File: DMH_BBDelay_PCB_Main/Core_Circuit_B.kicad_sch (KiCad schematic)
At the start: 70 parts, among them Q8 J113, SW1 SW_DPDT_OnOffOn_x2, SW2 SW_DPDT_x2, SW4 SW_SPDT, U5 TL074, U6 TL074, U7 V3205, U8 CD4046, U9 40106

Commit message: Re-implemented Ping Pong mode with CD4053
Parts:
- removed SW1: SW_DPDT_OnOffOn_x2, SynthStuff:Toggle_Switch_2_Poles_TE, symbol SynthStuff:SW_DPDT_OnOffOn_x2
- added R170: 100k, Resistor_THT:R_Axial_DIN0207_L6.3mm_D2.5mm_P7.62mm_Horizontal, symbol Device:R_US
- added SW1: SW_SPDT, symbol Switch:SW_SPDT
- added U18: CD4053B, Package_DIP:DIP-16_W7.62mm_Socket, symbol Analog_Switch:CD4053B
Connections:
- net +12V: now also R170.2, U18.16 (VDD)
- net -12V: now also U18.7 (VEE)
- net GND: now also SW1.1 (A), U18.6 (INH), U18.8 (VSS)
- net W_B_Out_m: now also U18.1 (B1), U18.12 (A0)
- net D_B_m renamed B_In_Buff_m
- net B_In_Buff_m: now also U18.3 (C1); no longer R25.1
- new net B_In_Buff_Sw_m: R25.1, U18.4 (C)
- new net PP_Sw_c: SW1.2 (B)
- new net PP_Sw_m: R170.1, U18.10 (S2), U18.11 (S1), U18.9 (S3)
- new net VCA_FB_A_In_m: U18.14 (A)
- new net VCA_FB_B_In_m: U18.15 (B)
- new net W_A_Out_m: U18.13 (A1), U18.2 (B0)
- no-connect marks 13 -> 15
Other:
- moved on the sheet: C30, C31, C33, C34, D16, D17, D18, R157, R158, R159, SW2B, U5E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

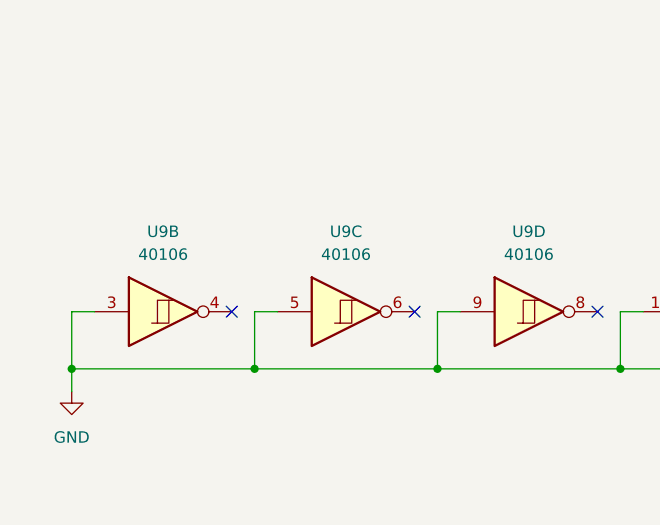
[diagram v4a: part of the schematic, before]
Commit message: Added schmit triggers to inhibt CV input paths
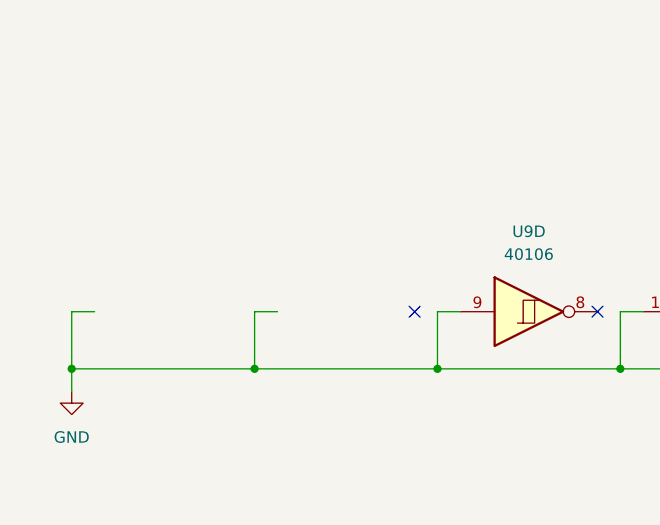
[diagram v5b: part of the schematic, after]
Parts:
- removed unit 2 of U9
- removed unit 3 of U9
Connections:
- no-connect marks 15 -> 14
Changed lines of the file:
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@@
 	)
 	(no_connect
-		(at 36.83 254)
-	)
-	(no_connect
 		(at 241.3 226.06)
 	)
@@
 	)
 	(symbol
-		(lib_id "4xxx:40106")
-		(at 29.21 254 0)
-		(unit 2)
-		(body_style 1)
-		(exclude_from_sim no)
-		(in_bom yes)
-		(on_board yes)
-		(in_pos_files yes)
-		(dnp no)
-		(fields_autoplaced yes)
-		(property "Reference" "U9"
-			(at 29.21 245.11 0)
-			(show_name no)
-			(do_not_autoplace no)
-			(effects
-				(font
-					(size 1.27 1.27)
-				)
-			)
-		)
-		(property "Value" "40106"
-			(at 29.21 247.65 0)
-			(show_name no)
-			(do_not_autoplace no)
-			(effects
-				(font
-					(size 1.27 1.27)
-				)
-			)
-		)
-		(property "Footprint" "Package_DIP:DIP-14_W7.62mm_Socket"
-			(at 29.21 254 0)
-			(hide yes)
-			(show_name no)
-			(do_not_autoplace no)
-			(effects
-				(font
-					(size 1.27 1.27)
-				)
-			)
-		)
-		(property "Datasheet" "https://assets.nexperia.com/documents/data-sheet/HEF40106B.pdf"
-			(at 29.21 254 0)
-			(hide yes)
-			(show_name no)
-			(do_not_autoplace no)
-			(effects
-				(font
-					(size 1.27 1.27)
-				)
-			)
-		)
-		(property "Description" "Hex Schmitt trigger inverter"
-			(at 29.21 254 0)
-			(hide yes)
-			(show_name no)
-			(do_not_autoplace no)
-			(effects
-				(font
-					(size 1.27 1.27)
-				)
-			)
-		)
-		(pin "3"
-		)
-		(pin "11"
-		)
-		(pin "9"
-		)
-		(pin "12"
-		)
-		(pin "2"
-		)
-		(pin "6"
-		)
-		(pin "13"
-		)
-		(pin "14"
-		)
-		(pin "4"
-		)
-		(pin "8"
-		)
-		(pin "1"
-		)
-		(pin "5"
-		)
-		(pin "10"
-		)
-		(pin "7"
-		)
-		(instances
-			(project "DMH_BBDelay_PCB_Main"
-				(path "/58f4306d-5387-4983-bb08-41a2313fd315/53120047-129a-4e0f-876f-6cafa2f18733"
-					(reference "U9")
-					(unit 2)
-				)
-			)
-		)
-	)
-	(symbol
 		(lib_id "power:+5V")
 		(at 140.97 78.74 0)
@@
 				)
 			)
-		)
-	)
-	(symbol
-		(lib_id "4xxx:40106")
-		(at 49.53 254 0)
-		(unit 3)
-		(body_style 1)
-		(exclude_from_sim no)
-		(in_bom yes)
-		(on_board yes)
-		(in_pos_files yes)
-		(dnp no)
-		(fields_autoplaced yes)
-		(property "Reference" "U9"
-			(at 49.53 245.11 0)
-			(show_name no)
-			(do_not_autoplace no)
-			(effects
-				(font
-					(size 1.27 1.27)
-				)
-			)
-		)
-		(property "Value" "40106"
-			(at 49.53 247.65 0)
-			(show_name no)
-			(do_not_autoplace no)
-			(effects
-				(font
-					(size 1.27 1.27)
-				)
-			)
-		)
-		(property "Footprint" "Package_DIP:DIP-14_W7.62mm_Socket"
-			(at 49.53 254 0)
-			(hide yes)
-			(show_name no)
-			(do_not_autoplace no)
-			(effects
-				(font
-					(size 1.27 1.27)
-				)
-			)
-		)
-		(property "Datasheet" "https://assets.nexperia.com/documents/data-sheet/HEF40106B.pdf"
-			(at 49.53 254 0)
-			(hide yes)
-			(show_name no)
-			(do_not_autoplace no)
-			(effects
-				(font
-					(size 1.27 1.27)
-				)
-			)
-		)
-		(property "Description" "Hex Schmitt trigger inverter"
-			(at 49.53 254 0)
-			(hide yes)
-			(show_name no)
-			(do_not_autoplace no)
-			(effects
-				(font
-					(size 1.27 1.27)
-				)
-			)
-		)
-		(pin "3"
-		)
-		(pin "11"
-		)
-		(pin "9"
-		)
-		(pin "12"
-		)
-		(pin "2"
-		)
-		(pin "6"
-		)
-		(pin "13"
-		)
-		(pin "14"
-		)
-		(pin "4"
-		)
-		(pin "8"
-		)
-		(pin "1"
-		)
-		(pin "5"
-		)
-		(pin "10"
-		)
-		(pin "7"
-		)
-		(instances
-			(project "DMH_BBDelay_PCB_Main"
-				(path "/58f4306d-5387-4983-bb08-41a2313fd315/53120047-129a-4e0f-876f-6cafa2f18733"
-					(reference "U9")
-					(unit 3)
-				)
-			)

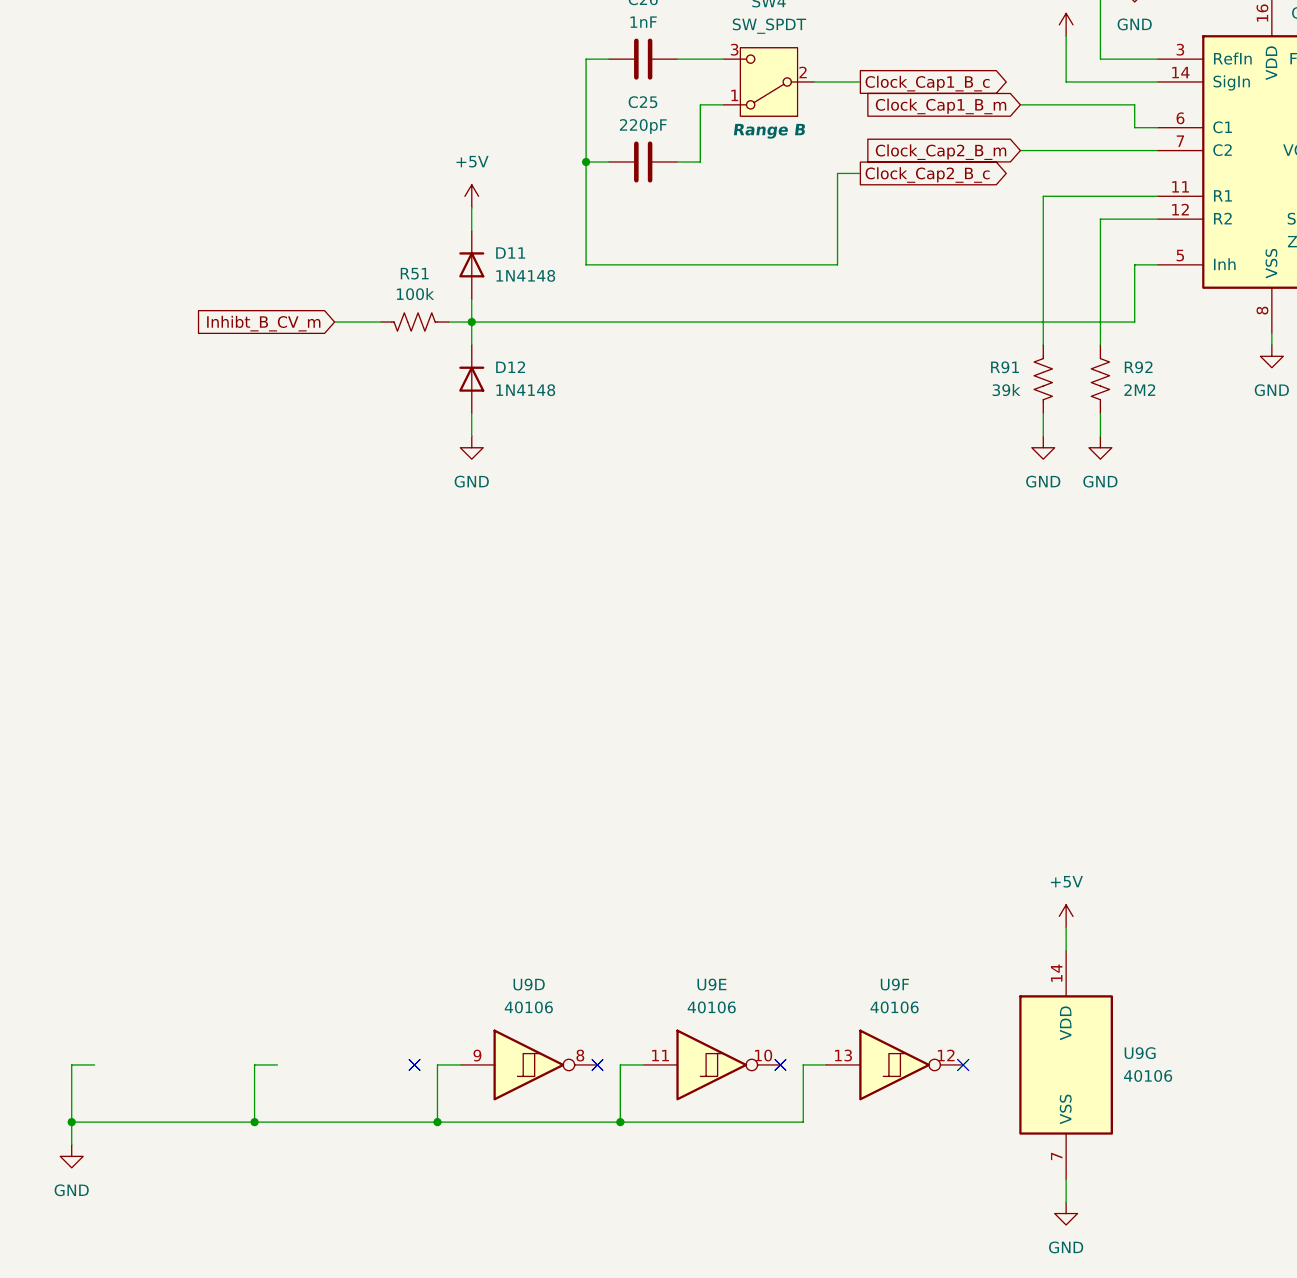
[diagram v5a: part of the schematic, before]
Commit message: Schmitt triggers added to Inhibt CV input paths
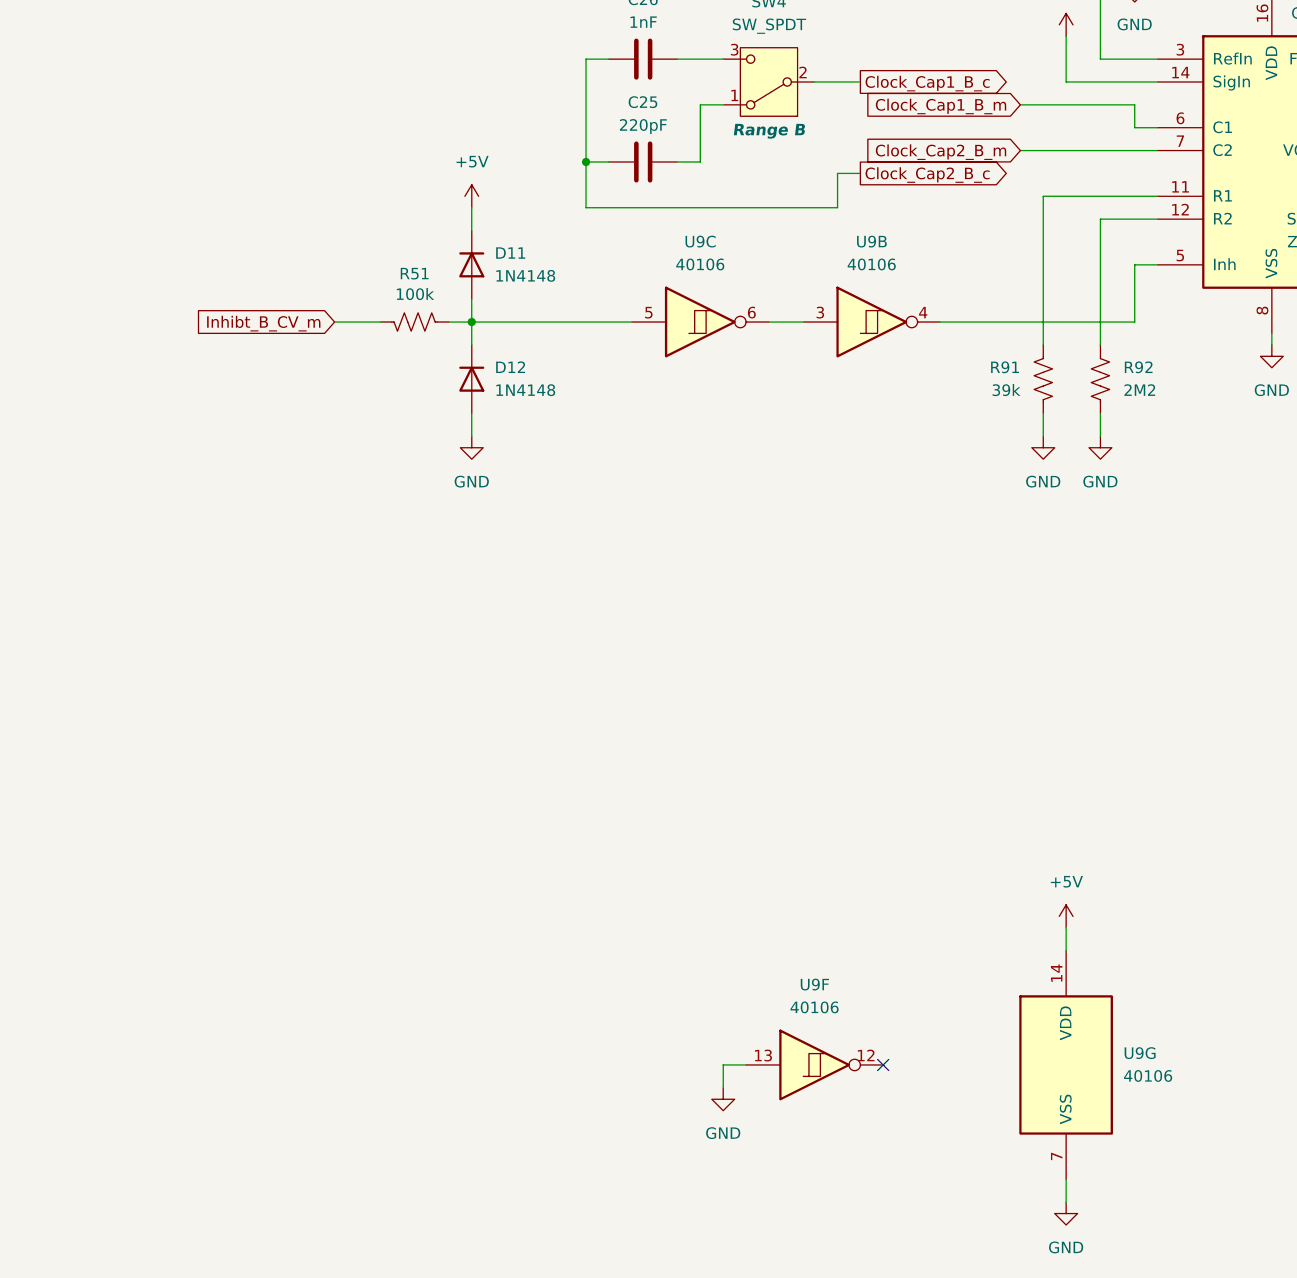
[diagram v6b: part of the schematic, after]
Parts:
- removed unit 4 of U9
- removed unit 5 of U9
- added unit 3 of U9
- added unit 2 of U9
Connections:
- net at D11.2 (A), D12.1 (K), R51.2: now also U9.5; no longer U8.5 (Inh)
- new net: U9.3, U9.6
- new net: U8.5 (Inh), U9.4
- no-connect marks 14 -> 11
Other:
- moved on the sheet: U9F

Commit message: Added TRS jacks to IO page
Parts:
- added R172: 100k, Resistor_THT:R_Axial_DIN0207_L6.3mm_D2.5mm_P7.62mm_Horizontal, symbol Device:R_US
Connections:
- net GND: now also R172.1
- net Inhibt_B_CV_m: now also R172.2
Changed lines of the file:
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@@
 	)
 	(junction
+		(at 50.8 171.45)
+		(diameter 0)
+		(color 0 0 0 0)
+	)
+	(junction
 		(at 250.19 149.86)
 		(diameter 0)
@@
 	(wire
 		(pts
-			(xy 48.26 171.45) (xy 53.34 171.45)
+			(xy 48.26 171.45) (xy 50.8 171.45)
 		)
 		(stroke
@@
 	(wire
 		(pts
+			(xy 50.8 171.45) (xy 50.8 173.99)
+		)
+		(stroke
+			(width 0)
+			(type default)
+		)
+	)
+	(wire
+		(pts
 			(xy 270.51 152.4) (xy 270.51 154.94)
 		)
@@
 	(wire
 		(pts
+			(xy 50.8 181.61) (xy 50.8 184.15)
+		)
+		(stroke
+			(width 0)
+			(type default)
+		)
+	)
+	(wire
+		(pts
 			(xy 209.55 218.44) (xy 215.9 218.44)
 		)
@@
 	(wire
 		(pts
+			(xy 50.8 171.45) (xy 53.34 171.45)
+		)
+		(stroke
+			(width 0)
+			(type default)
+		)
+	)
+	(wire
+		(pts
 			(xy 280.67 34.29) (xy 355.6 34.29)
 		)
@@
 	)
 	(symbol
+		(lib_id "Device:R_US")
+		(at 50.8 177.8 0)
+		(mirror x)
+		(unit 1)
+		(body_style 1)
+		(exclude_from_sim no)
+		(in_bom yes)
+		(on_board yes)
+		(in_pos_files yes)
+		(dnp no)
+		(property "Reference" "R172"
+			(at 46.355 178.689 0)
+			(show_name no)
+			(do_not_autoplace no)
+			(effects
+				(font
+					(size 1.27 1.27)
+				)
+			)
+		)
+		(property "Value" "100k"
+			(at 46.355 176.403 0)
+			(show_name no)
+			(do_not_autoplace no)
+			(effects
+				(font
+					(size 1.27 1.27)
+				)
+			)
+		)
+		(property "Footprint" "Resistor_THT:R_Axial_DIN0207_L6.3mm_D2.5mm_P7.62mm_Horizontal"
+			(at 51.816 177.546 90)
+			(hide yes)
+			(show_name no)
+			(do_not_autoplace no)
+			(effects
+				(font
+					(size 1.27 1.27)
+				)
+			)
+		)
+		(property "Datasheet" ""
+			(at 50.8 177.8 0)
+			(hide yes)
+			(show_name no)
+			(do_not_autoplace no)
+			(effects
+				(font
+					(size 1.27 1.27)
+				)
+			)
+		)
+		(property "Description" "Resistor, US symbol"
+			(at 50.8 177.8 0)
+			(hide yes)
+			(show_name no)
+			(do_not_autoplace no)
+			(effects
+				(font
+					(size 1.27 1.27)
+				)
+			)
+		)
+		(pin "2"
+		)
+		(pin "1"
+		)
+		(instances
+			(project "DMH_BBDelay_PCB_Main"
+				(path "/58f4306d-5387-4983-bb08-41a2313fd315/53120047-129a-4e0f-876f-6cafa2f18733"
+					(reference "R172")
+					(unit 1)
+				)
+			)
+		)
+	)
+	(symbol
 		(lib_id "power:-12V")
 		(at 349.25 242.57 180)
@@
 					(unit 1)
 				)
+			)
+		)
+	)
+	(symbol
+		(lib_id "power:GND")
+		(at 50.8 184.15 0)
+		(unit 1)
+		(body_style 1)
+		(exclude_from_sim no)
+		(in_bom yes)
+		(on_board yes)
+		(in_pos_files yes)
+		(dnp no)
+		(fields_autoplaced yes)
+		(property "Reference" "#PWR0201"
+			(at 50.8 190.5 0)
+			(hide yes)
+			(show_name no)
+			(do_not_autoplace no)
+			(effects
+				(font
+					(size 1.27 1.27)
+				)
+			)
+		)
+		(property "Value" "GND"
+			(at 50.8 189.23 0)
+			(show_name no)
+			(do_not_autoplace no)
+			(effects
+				(font
+					(size 1.27 1.27)
+				)
+			)
+		)
+		(property "Footprint" ""
+			(at 50.8 184.15 0)
+			(hide yes)
+			(show_name no)
+			(do_not_autoplace no)
+			(effects
+				(font
+					(size 1.27 1.27)
+				)
+			)
+		)
+		(property "Datasheet" ""
+			(at 50.8 184.15 0)
+			(hide yes)
+			(show_name no)
+			(do_not_autoplace no)
+			(effects
+				(font
+					(size 1.27 1.27)
+				)
+			)
+		)
+		(property "Description" "Power symbol creates a global label with name \"GND\" , ground"
+			(at 50.8 184.15 0)
+			(hide yes)
+			(show_name no)
+			(do_not_autoplace no)
+			(effects
+				(font
+					(size 1.27 1.27)
+				)
+			)
+		)
+		(pin "1"
+		)
+		(instances
+			(project "DMH_BBDelay_PCB_Main"
+				(path "/58f4306d-5387-4983-bb08-41a2313fd315/53120047-129a-4e0f-876f-6cafa2f18733"
+					(reference "#PWR0201")
+					(unit 1)
+				)
